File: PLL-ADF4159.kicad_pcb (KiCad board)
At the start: 4 copper layers, 48.5 x 38.2 mm, 66 parts, among them IC1 ADF4159CCPZ, J1 Power_and_Data, J3 External_VCO_RF, U1 LT3045IMSE_PBF, U2 ADP150AUJZ-3.3-R7, U3 ADP150AUJZ-3.0-R7, U4 ADP150AUJZ-1.8-R7, U6 RRA78610-QAJ

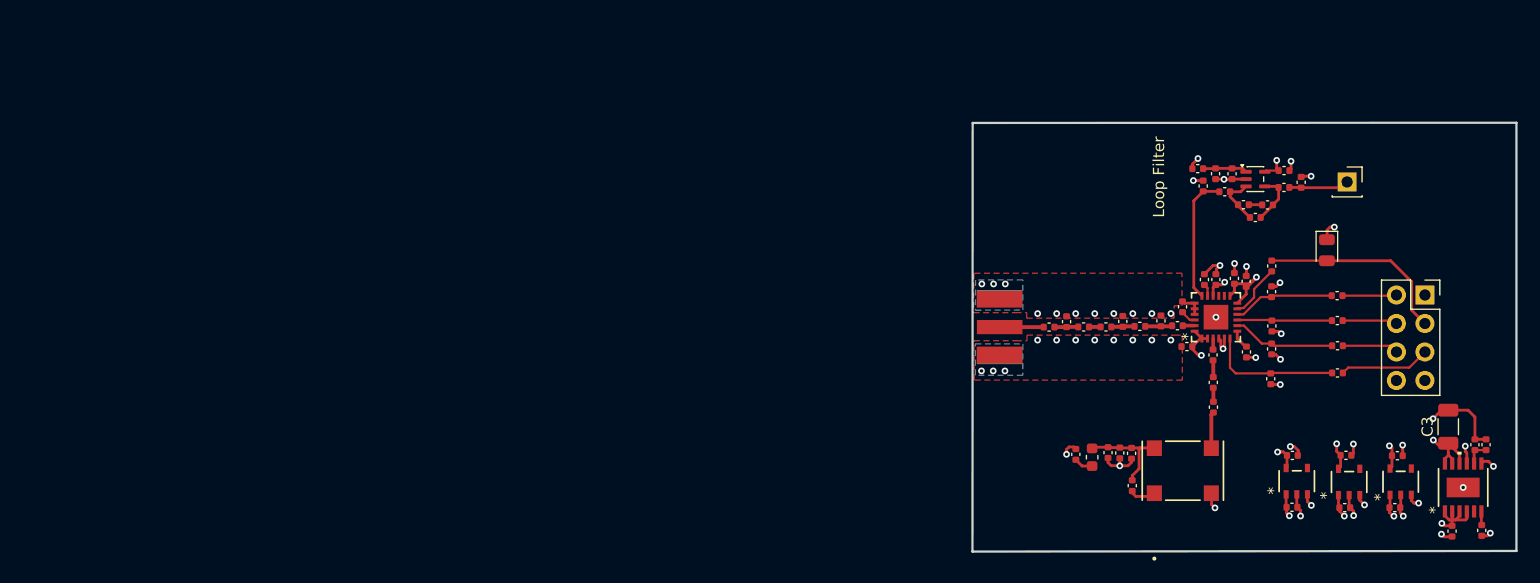
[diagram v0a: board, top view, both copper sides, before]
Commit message: Complete and adjust the PCB based on advisor's advice and manufacturer in-stock parts
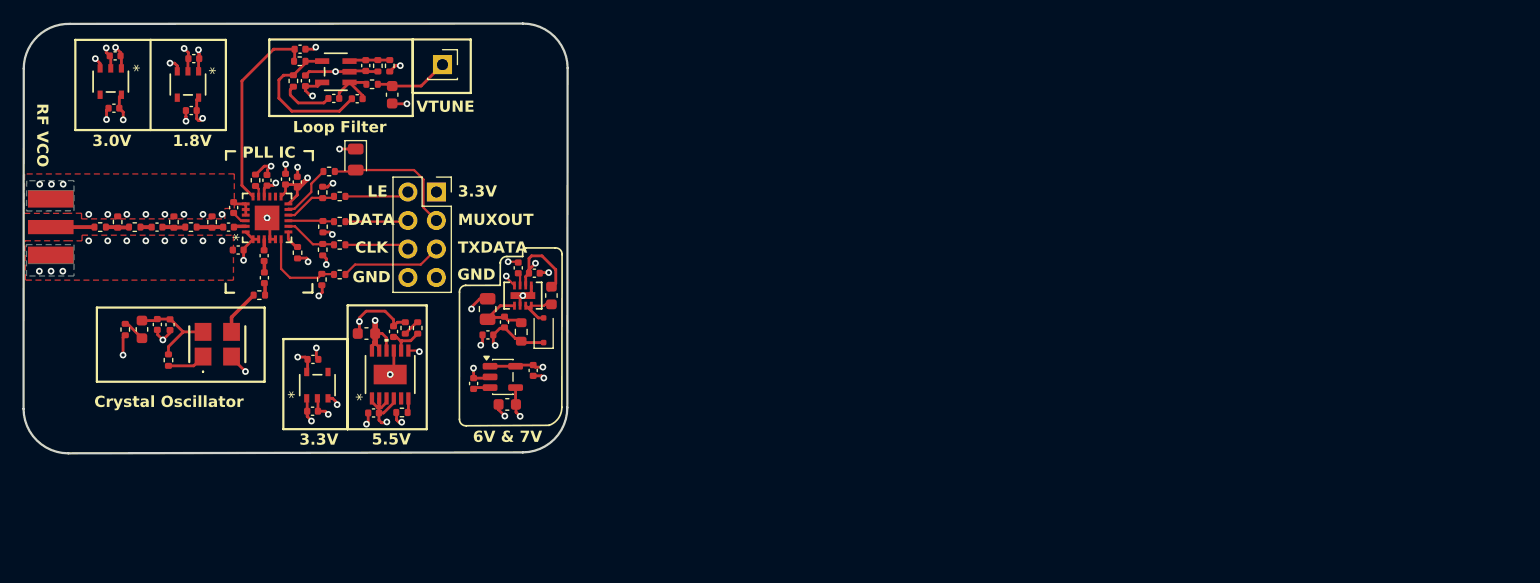
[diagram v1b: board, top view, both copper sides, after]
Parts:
- removed C19, C24: 1uF, Capacitor_SMD:C_0402_1005Metric
- removed C20: 96.5pF, Capacitor_SMD:C_0402_1005Metric
- removed C21: 215pF, Capacitor_SMD:C_0402_1005Metric
- removed C22: 739pF, Capacitor_SMD:C_0402_1005Metric
- removed C23: 25.9pF, Capacitor_SMD:C_0402_1005Metric
- removed C8: 10pF, Capacitor_SMD:C_0402_1005Metric
- removed R26, R27: 47k, Capacitor_SMD:C_0402_1005Metric
- removed R28: 220, Capacitor_SMD:C_0402_1005Metric
- removed R29: 1k, Capacitor_SMD:C_0402_1005Metric
- removed R30: 2.55k, Capacitor_SMD:C_0402_1005Metric
- removed XTAL1: CWX813-100.0M, OSC-CWX813:CWX813-100.0M_CNW-L
- added C28: 4.7uF, Capacitor_SMD:C_0402_1005Metric, F.Cu at (122.0, 68.4)
- added C29: 22pF, Capacitor_SMD:C_0402_1005Metric, F.Cu at (119.3, 72.8)
- added C30: 4.7uF, Capacitor_SMD:C_0402_1005Metric, F.Cu at (120.5, 67.9)
- added C31: 4.7uF, Capacitor_SMD:C_0402_1005Metric, F.Cu at (117.8, 73.9)
- added C32: 0.1uF, Capacitor_SMD:C_0402_1005Metric, F.Cu at (116.5, 78.2)
- added C33: 10uF, Capacitor_SMD:C_0603_1608Metric, F.Cu at (119.5, 80.1)
- added C34: 1uF, Capacitor_SMD:C_0402_1005Metric, F.Cu at (121.9, 77.1)
- added C35: 1uF, Capacitor_SMD:C_0402_1005Metric, F.Cu at (106.9, 49.9)
- added C36: 1uF, Capacitor_SMD:C_0402_1005Metric, F.Cu at (101.5, 51.2)
- added C37: 100pF, Capacitor_SMD:C_0402_1005Metric, F.Cu at (101.1, 48.4)
- added C38: 27nF, Capacitor_SMD:C_0402_1005Metric, F.Cu at (104.1, 52.8)
- added C39: 160pF, Capacitor_SMD:C_0402_1005Metric, F.Cu at (106.2, 52.8)
- added C40: 42pF, Capacitor_SMD:C_0603_1608Metric, F.Cu at (109.3, 52.5)
- added D2: PMEG6010CEJ, Diode_SMD:D_SOD-323F, F.Cu at (122.8, 73.5)
- added G***: LOGO, LOGO, B.Cu at (99.7, 65.2)
- added L1: 6.8uH, Inductor_SMD:L_0603_1608Metric, F.Cu at (123.5, 70.4)
- added R1: 189k, Resistor_SMD:R_0603_1608Metric, F.Cu at (120.8, 73.6)
- added R33: 47k, Resistor_SMD:R_0402_1005Metric, F.Cu at (109.1, 49.9)
- added R34: 47k, Resistor_SMD:R_0402_1005Metric, F.Cu at (108.0, 49.9)
- added R35: 220, Resistor_SMD:R_0402_1005Metric, F.Cu at (101.0, 49.5)
- added R36: 383, Resistor_SMD:R_0402_1005Metric, F.Cu at (100.5, 51.3)
- added R37: 1k, Resistor_SMD:R_0402_1005Metric, F.Cu at (107.5, 51.6)
- added R4: 5K, Resistor_SMD:R_0402_1005Metric, F.Cu at (110.4, 73.3)
- added R5: 56k, Resistor_SMD:R_0805_2012Metric, F.Cu at (117.8, 71.6)
- added U5: LT8330IDDB-TRPBF, symbols:DDB_05-08-1702_ADI-L, F.Cu at (120.9, 70.4)
- added U7: LK112M60TR, Package_TO_SOT_SMD:SOT-23-5, F.Cu at (119.1, 77.6)
- added Y1: SIT8008BI-32-33E-100.000000, symbols:SiT8921BM3233N127872000, F.Cu at (93.7, 74.7)
- C3: value 12uF -> 22uF; footprint Capacitor_SMD:C_1206_3216Metric -> Capacitor_SMD:C_0603_1608Metric
- C9: value 10nF -> 100nF
- R10, R12, R13, R14, R15, R16, R17, R18, R19, R2, R31, R32, R8, R9: footprint Capacitor_SMD:C_0402_1005Metric -> Resistor_SMD:R_0402_1005Metric
- R20: value 8.6 -> 150; footprint Capacitor_SMD:C_0402_1005Metric -> Resistor_SMD:R_0402_1005Metric
- R21, R22: value 142 -> 8.2; footprint Capacitor_SMD:C_0402_1005Metric -> Resistor_SMD:R_0402_1005Metric
- R23, R24: value 150.5 -> 150; footprint Capacitor_SMD:C_0402_1005Metric -> Resistor_SMD:R_0402_1005Metric
- R25: value 37.4 -> 39; footprint Capacitor_SMD:C_0402_1005Metric -> Resistor_SMD:R_0402_1005Metric
- R3: value 55k -> 50k; footprint Capacitor_SMD:C_0402_1005Metric -> Resistor_SMD:R_0402_1005Metric
- R7: value 91R -> 91; footprint Capacitor_SMD:C_0402_1005Metric -> Resistor_SMD:R_0402_1005Metric
- U6: value RRA78610-QAJ -> TLV9061IDBVR; footprint Package_TO_SOT_SMD:SOT-353_SC-70-5 -> symbols:DBV5_TEX
- moved C5 116.8 mm to (84.6, 49.0), turned to 180 degrees
- moved U3 116.0 mm to (84.2, 51.3), turned to -90 degrees
- moved C6 114.3 mm to (91.6, 49.3), turned to 180 degrees
- moved C26 114.1 mm to (84.5, 53.7), turned to 180 degrees
- moved U4 113.8 mm to (91.1, 51.6), turned to -90 degrees
- moved C27 111.8 mm to (91.4, 53.9), turned to 180 degrees
- moved C2 97.9 mm to (109.4, 73.6)
- moved R2 96.8 mm to (110.2, 80.8), turned to 0 degrees
- moved C3 96.8 mm to (107.0, 73.8), turned to 180 degrees
- moved C1 96.7 mm to (107.6, 80.9), turned to 180 degrees
- moved U1 96.2 mm to (109.1, 77.4)
- moved R3 94.8 mm to (111.6, 73.3)
- moved R14 89.4 mm to (104.6, 65.9)
- moved R31 89.4 mm to (104.6, 68.5)
- moved R13 89.4 mm to (104.6, 63.8)
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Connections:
- C1 pad 1: /+6.5V_RAW -> /Power Supply/6V
- C3 pad 1: /Loop Filter/5.5V -> /Power Supply/5.5V
- C4 pad 1: /+6.5V_RAW -> /Power Supply/5.5V
- C5 pad 1: /+6.5V_RAW -> /+3.3V_RAW
- C6 pad 1: /+6.5V_RAW -> /+3.3V_RAW
- J1 pad 1: /+6.5V_RAW -> /+3.3V_RAW
- R3 pad 2: GND -> Net-(R3-Pad2)
- U1 pad 1: /+6.5V_RAW -> /Power Supply/6V
- U1 pad 10: /Loop Filter/5.5V -> /Power Supply/5.5V
- U1 pad 11: /Loop Filter/5.5V -> /Power Supply/5.5V
- U1 pad 12: /Loop Filter/5.5V -> /Power Supply/5.5V
- U1 pad 2: /+6.5V_RAW -> /Power Supply/6V
- U1 pad 3: /+6.5V_RAW -> /Power Supply/6V
- U1 pad 4: /+6.5V_RAW -> /Power Supply/6V
- U1 pad 7: /+6.5V_RAW -> /Power Supply/6V
- U2 pad 1: /+6.5V_RAW -> /Power Supply/5.5V
- U2 pad 3: /+6.5V_RAW -> /Power Supply/5.5V
- U3 pad 1: /+6.5V_RAW -> /+3.3V_RAW
- U3 pad 3: /+6.5V_RAW -> /+3.3V_RAW
- U4 pad 1: /+6.5V_RAW -> /+3.3V_RAW
- U4 pad 3: /+6.5V_RAW -> /+3.3V_RAW
- U6 pad 5: /Loop Filter/5.5V -> /Power Supply/5.5V
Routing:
- net /+6.5V_RAW: track 17.4 -> 0.00 mm, vias 8 -> 0
- net GND: track 44.7 -> 61.1 mm, vias 49 -> 54
- net /+3.3V_RAW: track 0.00 -> 16.2 mm, vias 0 -> 6
- net /Power Supply/5.5V: track 0.00 -> 12.1 mm, vias 0 -> 4
- net /Power Supply/7V: track 0.00 -> 11.3 mm, vias 0 -> 2
- net /Power Supply/6V: track 0.00 -> 11.0 mm, vias 0 -> 3
- net Net-(U6-IN-): track 4.60 -> 13.7 mm
- net /Loop Filter/5.5V: track 8.00 -> 0.00 mm, vias 2 -> 0
- net /ADF4159/CPOUT: track 11.4 -> 17.7 mm
- net Net-(U5-FBX): track 0.00 -> 5.88 mm
- net /MUXOUT: track 17.5 -> 12.5 mm
- net Net-(C38-Pad1): track 0.00 -> 4.72 mm
- net Net-(IC1-CLK): track 9.20 -> 4.78 mm
- net Net-(IC1-DATA): track 8.45 -> 4.12 mm
- net Net-(IC1-LE): track 9.11 -> 4.96 mm
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- added copper zone on In2.Cu, net /+3.3V_RAW
- added copper zone on In2.Cu, net /Power Supply/5.5V
- added copper zone on In2.Cu, net /Power Supply/6V
- added copper zone on In2.Cu, net /Power Supply/7V
- removed copper zone on In2.Cu, net /+6.5V_RAW
- removed copper zone on In2.Cu, net /Loop Filter/5.5V
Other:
- board size 48.5 x 38.2 mm -> 48.5 x 38.3 mm
- board text added: "1.8V"
- board text added: "3.0V"
- board text added: "3.3V"
- board text added: "5.5V"
- board text added: "6V & 7V"
- board text added: "CLK"
- board text added: "Crystal Oscillator"
- board text added: "DATA"
- board text added: "GND"
- board text added: "LE"
- board text added: "MUXOUT"
- board text added: "PLL IC"
- board text added: "RF VCO"
- board text added: "TXDATA"
- board text added: "VTUNE"
